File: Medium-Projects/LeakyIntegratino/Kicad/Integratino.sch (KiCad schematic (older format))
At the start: 8 parts

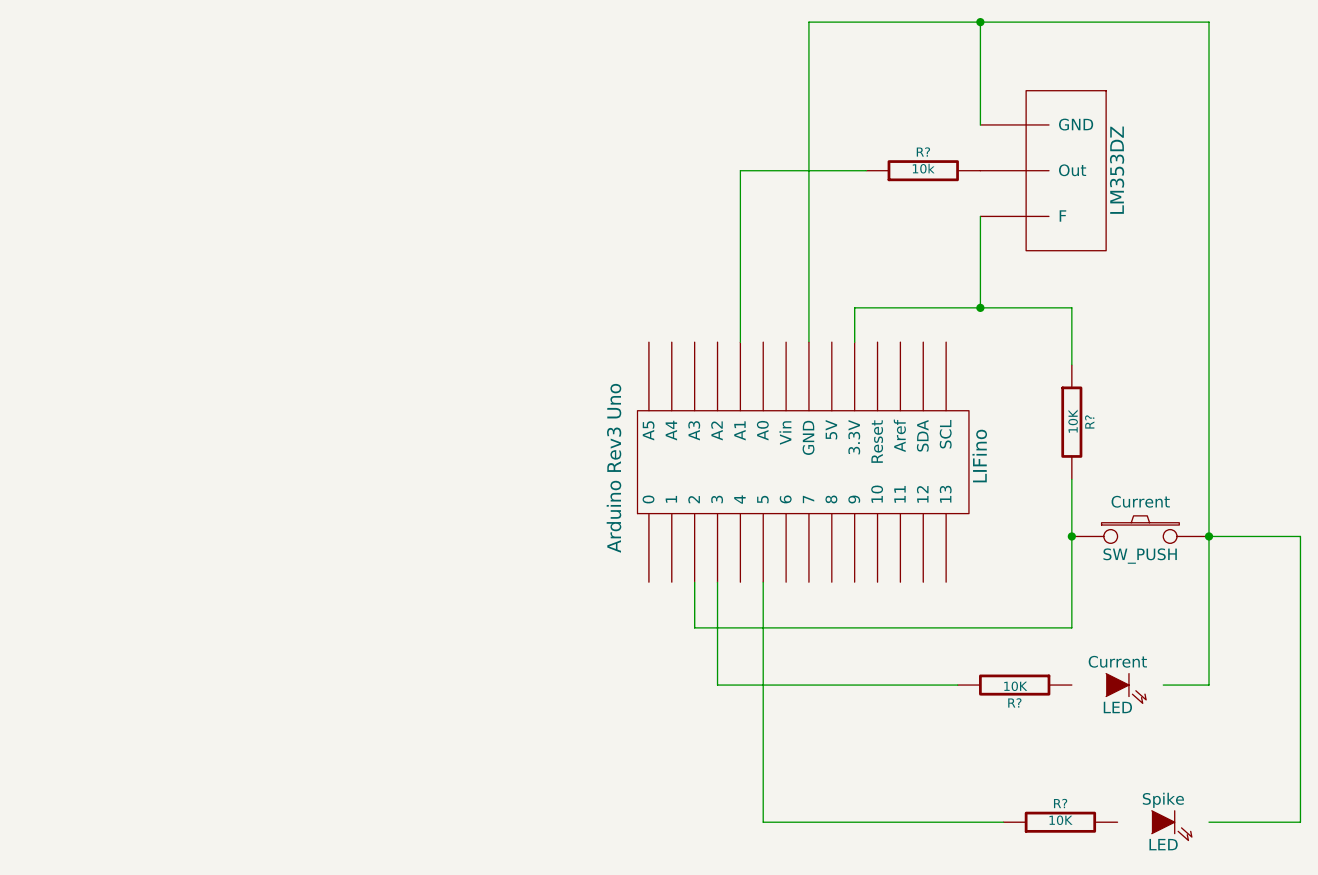
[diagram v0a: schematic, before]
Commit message: Integratino- updated circuit with analogical output
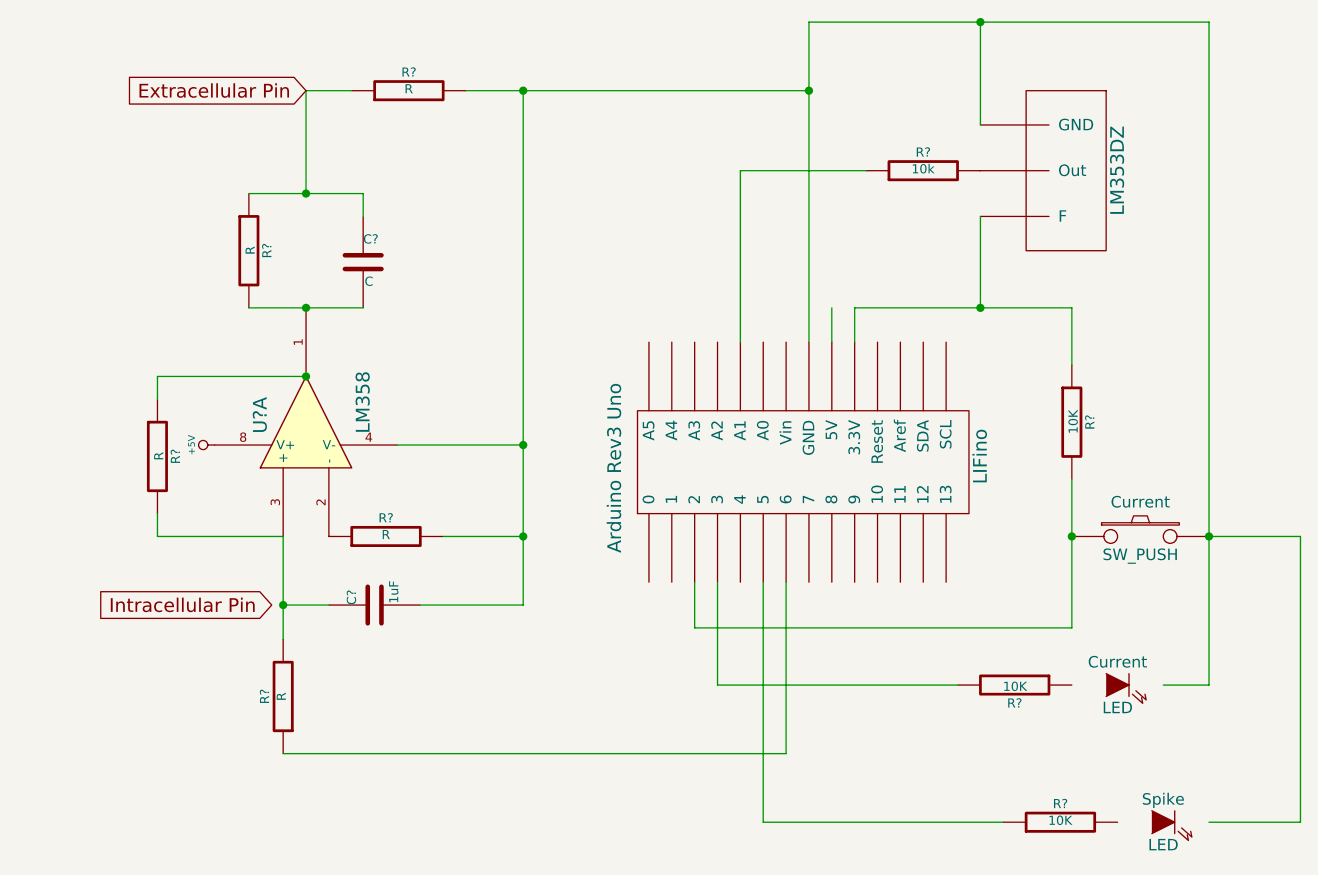
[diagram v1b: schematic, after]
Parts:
- added C?: 1uF, ~, symbol C
- added C?: C, ~, symbol C
- added R? (x5): R, ~, symbol R
- added U?: LM358, symbol LM358
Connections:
- net labels added: +5V, Extracellular Pin, Intracellular Pin
- wire segments 21 -> 40
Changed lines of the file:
@@
 LIBS:arduino_uno
+LIBS:Integratino-cache
 LIBS:Integratino-cache
 EELAYER 27 0
@@
 	1    0    0    -1
 $EndComp
-Wire Wire Line
-	4500 3450 4500 3300
-Wire Wire Line
-	4500 3300 5450 3300
-Wire Wire Line
-	5450 3300 5450 3550
-Wire Wire Line
-	3800 4500 3800 4700
-Wire Wire Line
-	3800 4700 5450 4700
 $Comp
 L SW_PUSH Current
@@
 	1    0    0    -1
 $EndComp
-Wire Wire Line
-	5450 4700 5450 4050
-Connection ~ 5450 4300
-Wire Wire Line
-	4300 2050 4300 3450
-Wire Wire Line
-	6050 2050 6050 4950
 $Comp
 L R R?
@@
 	1    0    0    -1
 $EndComp
-Connection ~ 6050 4300
-Wire Wire Line
-	3900 4500 3900 4950
-Wire Wire Line
-	4100 4500 4100 5550
 $Comp
 L LED Spike
@@
 	1    0    0    -1
 $EndComp
-Wire Wire Line
-	6450 5550 6450 4300
-Wire Wire Line
-	6450 4300 6050 4300
-Wire Wire Line
-	6050 4950 5850 4950
-Wire Wire Line
-	3900 4950 4950 4950
 $Comp
 L R R?
@@
 	0    -1   -1   0
 $EndComp
-Wire Wire Line
-	4100 5550 5150 5550
-Wire Wire Line
-	6050 5550 6450 5550
-Wire Wire Line
-	4300 2050 6050 2050
-Connection ~ 5050 3300
-Connection ~ 5050 2050
-Wire Wire Line
-	5050 2900 5050 3300
-Wire Wire Line
-	5050 2050 5050 2500
 $Comp
 L R R?
@@
 	0    -1   -1   0
 $EndComp
-Wire Wire Line
-	4000 3450 4000 2700
-Wire Wire Line
-	4000 2700 4550 2700
 $Comp
 L LM353DZ ~
@@
 	0    1    1    0
 $EndComp
+$Comp
+L R R?
+U 1 1 55566D09
+P 2000 5000
+F 0 "R?" V 2080 5000 40  0000 C CNN
+F 1 "R" V 2007 5001 40  0000 C CNN
+F 2 "~" V 1930 5000 30  0000 C CNN
+F 3 "~" H 2000 5000 30  0000 C CNN
+	1    2000 5000
+	-1   0    0    1
+$EndComp
+$Comp
+L C C?
+U 1 1 55566D18
+P 2400 4600
+F 0 "C?" H 2400 4700 40  0000 L CNN
+F 1 "1uF" H 2406 4515 40  0000 L CNN
+F 2 "~" H 2438 4450 30  0000 C CNN
+F 3 "~" H 2400 4600 60  0000 C CNN
+	1    2400 4600
+	0    -1   -1   0
+$EndComp
+$Comp
+L R R?
+U 1 1 55566F20
+P 1850 3050
+F 0 "R?" V 1930 3050 40  0000 C CNN
+F 1 "R" V 1857 3051 40  0000 C CNN
+F 2 "~" V 1780 3050 30  0000 C CNN
+F 3 "~" H 1850 3050 30  0000 C CNN
+	1    1850 3050
+	1    0    0    -1
+$EndComp
+$Comp
+L C C?
+U 1 1 55566F2F
+P 2350 3100
+F 0 "C?" H 2350 3200 40  0000 L CNN
+F 1 "C" H 2356 3015 40  0000 L CNN
+F 2 "~" H 2388 2950 30  0000 C CNN
+F 3 "~" H 2350 3100 60  0000 C CNN
+	1    2350 3100
+	1    0    0    -1
+$EndComp
+$Comp
+L R R?
+U 1 1 55567081
+P 2550 2350
+F 0 "R?" V 2630 2350 40  0000 C CNN
+F 1 "R" V 2557 2351 40  0000 C CNN
+F 2 "~" V 2480 2350 30  0000 C CNN
+F 3 "~" H 2550 2350 30  0000 C CNN
+	1    2550 2350
+	0    -1   -1   0
+$EndComp
+$Comp
+L LM358 U?
+U 1 1 5556762C
+P 2100 3800
+F 0 "U?" H 2050 4000 60  0000 L CNN
+F 1 "LM358" H 2050 3550 60  0000 L CNN
+F 2 "" H 2100 3800 60  0000 C CNN
+F 3 "" H 2100 3800 60  0000 C CNN
+	1    2100 3800
+	0    -1   -1   0
+$EndComp
+Wire Wire Line
+	4500 3450 4500 3300
+Wire Wire Line
+	4500 3300 5450 3300
+Wire Wire Line
+	5450 3300 5450 3550
+Wire Wire Line
+	3800 4500 3800 4700
+Wire Wire Line
+	3800 4700 5450 4700
+Wire Wire Line
+	5450 4700 5450 4050
+Connection ~ 5450 4300
+Wire Wire Line
+	4300 2050 4300 3450
+Wire Wire Line
+	6050 2050 6050 4950
+Connection ~ 6050 4300
+Wire Wire Line
+	3900 4500 3900 4950
+Wire Wire Line
+	4100 4500 4100 5550
+Wire Wire Line
+	6450 5550 6450 4300
+Wire Wire Line
+	6450 4300 6050 4300
+Wire Wire Line
+	6050 4950 5850 4950
+Wire Wire Line
+	3900 4950 4950 4950
+Wire Wire Line
+	4100 5550 5150 5550
+Wire Wire Line
+	6050 5550 6450 5550
+Wire Wire Line
+	4300 2050 6050 2050
+Connection ~ 5050 3300
+Connection ~ 5050 2050
+Wire Wire Line
+	5050 2900 5050 3300
+Wire Wire Line
+	5050 2050 5050 2500
+Wire Wire Line
+	4000 3450 4000 2700
+Wire Wire Line
+	4000 2700 4550 2700
+Wire Wire Line
+	2800 2350 4300 2350
+Connection ~ 4300 2350
+Wire Wire Line
+	4200 5250 4200 4500
+Wire Wire Line
+	3050 2350 3050 4600
+Wire Wire Line
+	2000 5250 4200 5250
+Connection ~ 2000 4600
+Connection ~ 2100 3300
+Wire Wire Line
+	1850 3300 2350 3300
+Wire Wire Line
+	1850 2800 2350 2800
+Wire Wire Line
+	2350 2800 2350 2900
+Connection ~ 2100 2800
+Wire Wire Line
+	2000 4300 2000 4750
+Wire Wire Line
+	4400 3450 4400 3300
+Wire Wire Line
+	2500 3900 3050 3900
+Connection ~ 3050 3900
+Wire Wire Line
+	2100 2350 2100 2800
+Wire Wire Line
+	2100 2350 2300 2350
+Connection ~ 3050 2350
+$Comp
+L R R?
+U 1 1 55567CC6
+P 2450 4300
+F 0 "R?" V 2530 4300 40  0000 C CNN
+F 1 "R" V 2457 4301 40  0000 C CNN
+F 2 "~" V 2380 4300 30  0000 C CNN
+F 3 "~" H 2450 4300 30  0000 C CNN
+	1    2450 4300
+	0    -1   -1   0
+$EndComp
+Wire Wire Line
+	2700 4300 3050 4300
+Connection ~ 3050 4300
+Wire Wire Line
+	2000 4600 2200 4600
+Wire Wire Line
+	3050 4600 2600 4600
+$Comp
+L +5V #PWR?
+U 1 1 55567646
+P 1700 3900
+F 0 "#PWR?" H 1700 3990 20  0001 C CNN
+F 1 "+5V" H 1700 4000 30  0000 C CNN
+F 2 "" H 1700 3900 60  0000 C CNN
+F 3 "" H 1700 3900 60  0000 C CNN
+	1    1700 3900
+	0    -1   -1   0
+$EndComp
+Wire Wire Line
+	2100 3600 1450 3600
+Wire Wire Line
+	1450 4300 2000 4300
+Connection ~ 2100 3600
+$Comp
+L R R?
+U 1 1 55567EFD
+P 1450 3950
+F 0 "R?" V 1530 3950 40  0000 C CNN
+F 1 "R" V 1457 3951 40  0000 C CNN
+F 2 "~" V 1380 3950 30  0000 C CNN
+F 3 "~" H 1450 3950 30  0000 C CNN
+	1    1450 3950
+	1    0    0    -1
+$EndComp
+Wire Wire Line
+	1450 3600 1450 3700
+Wire Wire Line
+	1450 4200 1450 4300
+Text GLabel 2100 2350 0    60   Input ~ 0
+Extracellular Pin
+Text GLabel 1950 4600 0    60   Input ~ 0
+Intracellular Pin
 $EndSCHEMATC

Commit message: updating everything
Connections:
- wire segments 40 -> 39
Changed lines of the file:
@@
 Sheet 1 1
 Title ""
-Date "15 may 2015"
+Date "16 may 2015"
 Rev ""
 Comp ""
@@
 	2000 4300 2000 4750
 Wire Wire Line
-	4400 3450 4400 3300
-Wire Wire Line
 	2500 3900 3050 3900
